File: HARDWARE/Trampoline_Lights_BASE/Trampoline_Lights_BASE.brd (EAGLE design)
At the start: 120.7 x 111.8 mm, 4 parts

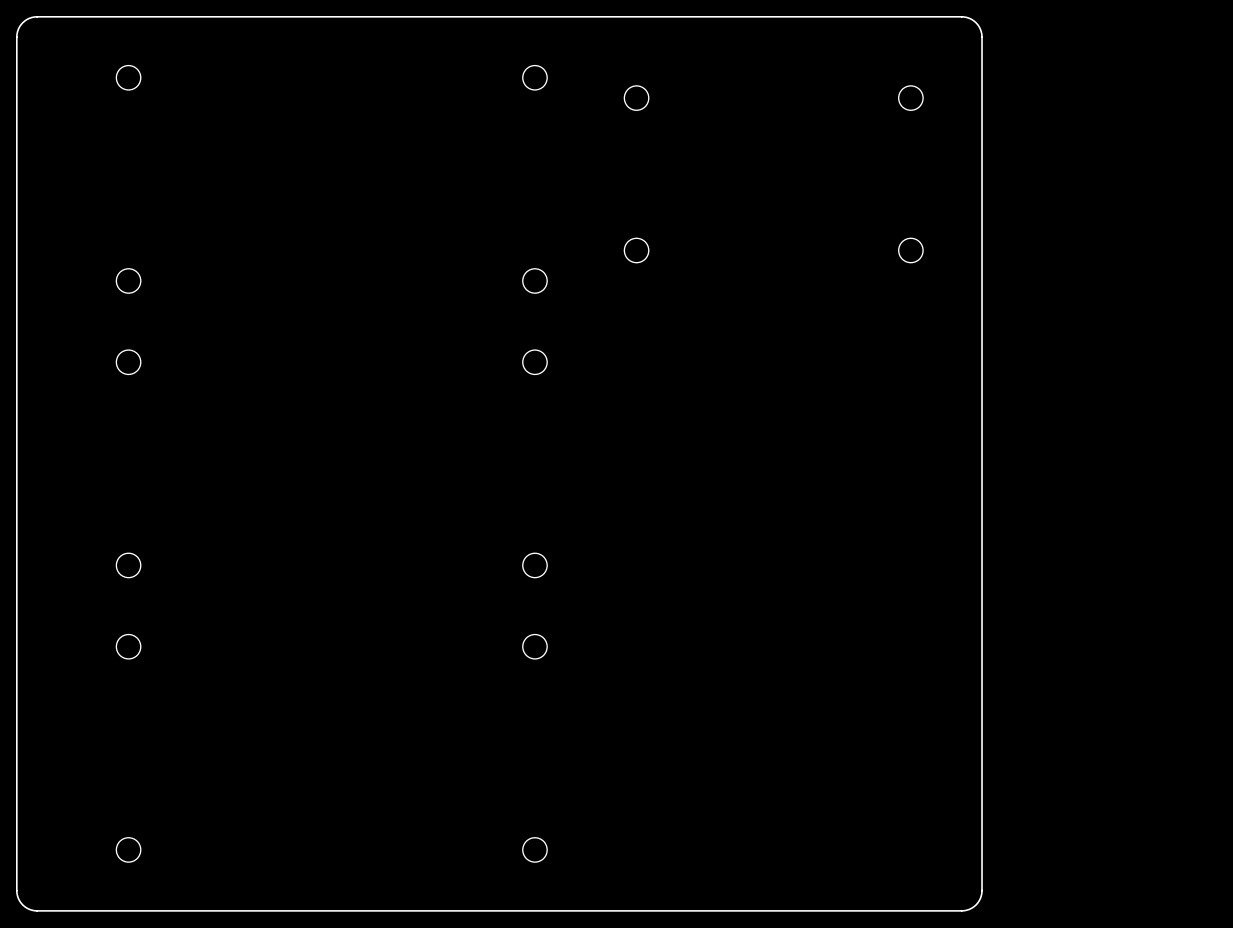
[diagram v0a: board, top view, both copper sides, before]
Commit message: Lights BASE - moved to BIG RED ENCLOSURE outer dimension
This should now fit into the SparkFun big red enclosure box

https://www.sparkfun.com/products/11366
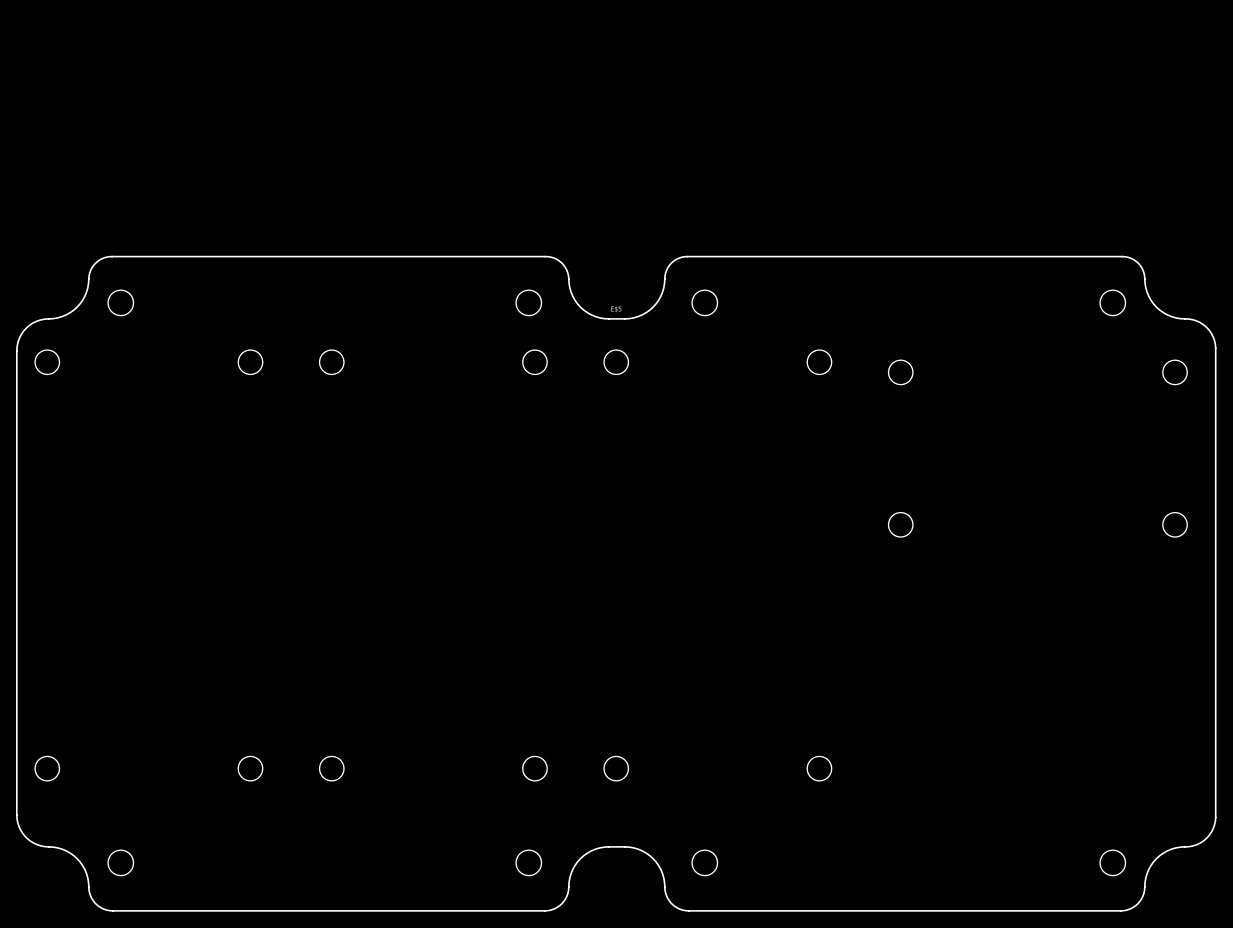
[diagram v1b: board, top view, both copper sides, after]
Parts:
- added E$5: (no value), SparkFun-Boards:FLANGED_RED_ENCLOSURE-DIMENSION
- moved E$3 71.8 mm to (87.6, 40.6), turned to 90 degrees
- moved E$4 47.6 mm to (128.3, 57.1)
- moved E$2 25.4 mm to (16.5, 40.6), turned to 90 degrees
- moved E$1 25.4 mm to (52.1, 40.6), turned to 90 degrees
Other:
- board size 120.7 x 111.8 mm -> 149.9 x 81.8 mm
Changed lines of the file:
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@@
 <board>
 <plain>
-<wire x1="118.11" y1="0" x2="2.54" y2="0" width="0.2032" layer="20"/>
-<wire x1="2.54" y1="0" x2="0" y2="2.54" width="0.2032" layer="20" curve="-90"/>
-<wire x1="0" y1="2.54" x2="0" y2="109.22" width="0.2032" layer="20"/>
-<wire x1="0" y1="109.22" x2="2.54" y2="111.76" width="0.2032" layer="20" curve="-90"/>
-<wire x1="2.54" y1="111.76" x2="118.11" y2="111.76" width="0.2032" layer="20"/>
-<wire x1="118.11" y1="111.76" x2="120.65" y2="109.22" width="0.2032" layer="20" curve="-90"/>
-<wire x1="120.65" y1="109.22" x2="120.65" y2="2.54" width="0.2032" layer="20"/>
-<wire x1="120.65" y1="2.54" x2="118.11" y2="0" width="0.2032" layer="20" curve="-90"/>
 </plain>
 <attributes>
@@
 </autorouter>
 <elements>
-<element name="E$1" library="simon_jumps" package="BEEFCAKE_RELAY" value="" x="36.83" y="20.32"/>
-<element name="E$2" library="simon_jumps" package="BEEFCAKE_RELAY" value="" x="36.83" y="55.88"/>
-<element name="E$3" library="simon_jumps" package="BEEFCAKE_RELAY" value="" x="36.83" y="91.44"/>
-<element name="E$4" library="simon_jumps" package="SIMON_JUMPS_LIGHT_BREAKOUT" value="" x="95.25" y="91.44" rot="R90"/>
+<element name="E$1" library="simon_jumps" package="BEEFCAKE_RELAY" value="" x="52.07" y="40.64" rot="R90"/>
+<element name="E$2" library="simon_jumps" package="BEEFCAKE_RELAY" value="" x="16.51" y="40.64" rot="R90"/>
+<element name="E$3" library="simon_jumps" package="BEEFCAKE_RELAY" value="" x="87.63" y="40.64" rot="R90"/>
+<element name="E$4" library="simon_jumps" package="SIMON_JUMPS_LIGHT_BREAKOUT" value="" x="128.27" y="57.15" rot="R90"/>
+<element name="E$5" library="SparkFun-Boards" package="FLANGED_RED_ENCLOSURE-DIMENSION" value="" x="74.93" y="41.91"/>
 </elements>
 <signals>
